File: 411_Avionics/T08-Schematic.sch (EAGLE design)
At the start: 41 parts, among them IC1 BQ24022, J1 USB-MICROB, J3 JST-PH-2-SMT-RA, U1 LP5907, U2 M25P10-AVMN6TP_TR, U3 LSM9DS0, U5 LTC1998, U6 ATMEGA32U4-AU, X1 8MHz

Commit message: Layout Review #1 With Andrew:
-changed all 0805 packages to 0603  (made a lot more room)
-made vias significantly smaller (made a lot more room)
-updated layout to reflect these changes, no DRC issues

We should consider hooking up the status pins of our battery charger to
LEDs.  Should also consider increasing the value of our current limiting
resistors from the processor.
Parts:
- C1, C10, C11, C12, C13, C14, C15, C16, C17, C18, C3, C4, C5, C6, C7, C8, C9: device rcl:C-EUC0805 -> rcl:C-EUC0603
- R1, R10, R11, R3, R4, R5, R6, R7, R8, R9: device rcl:R-US_R0805 -> rcl:R-US_R0603

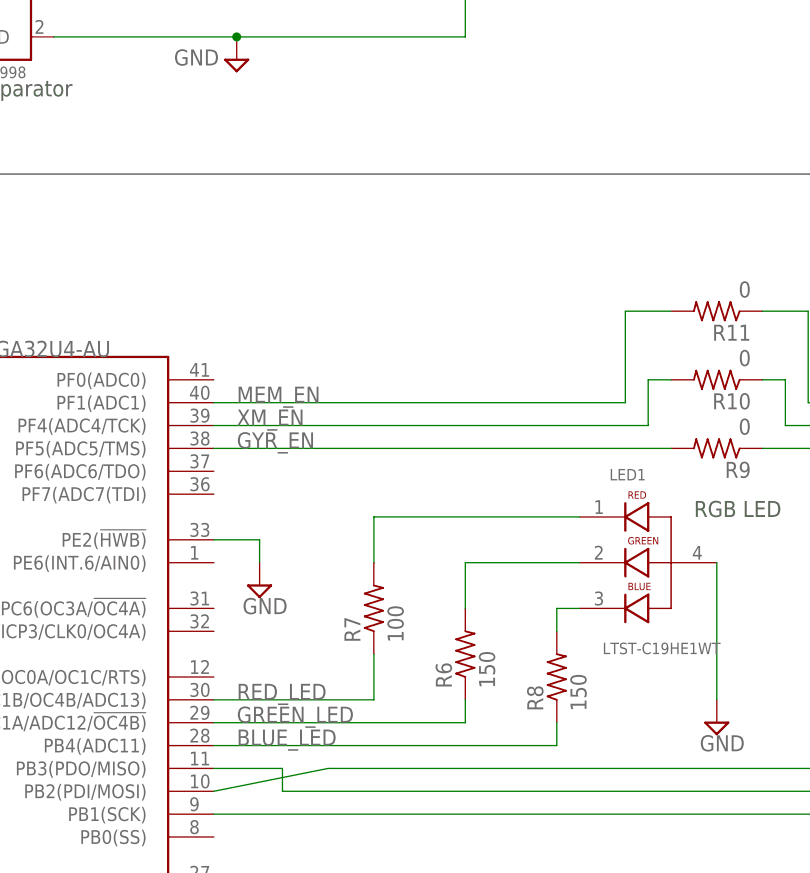
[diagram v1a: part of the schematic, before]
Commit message: Added 3-pin pad for firing circuit
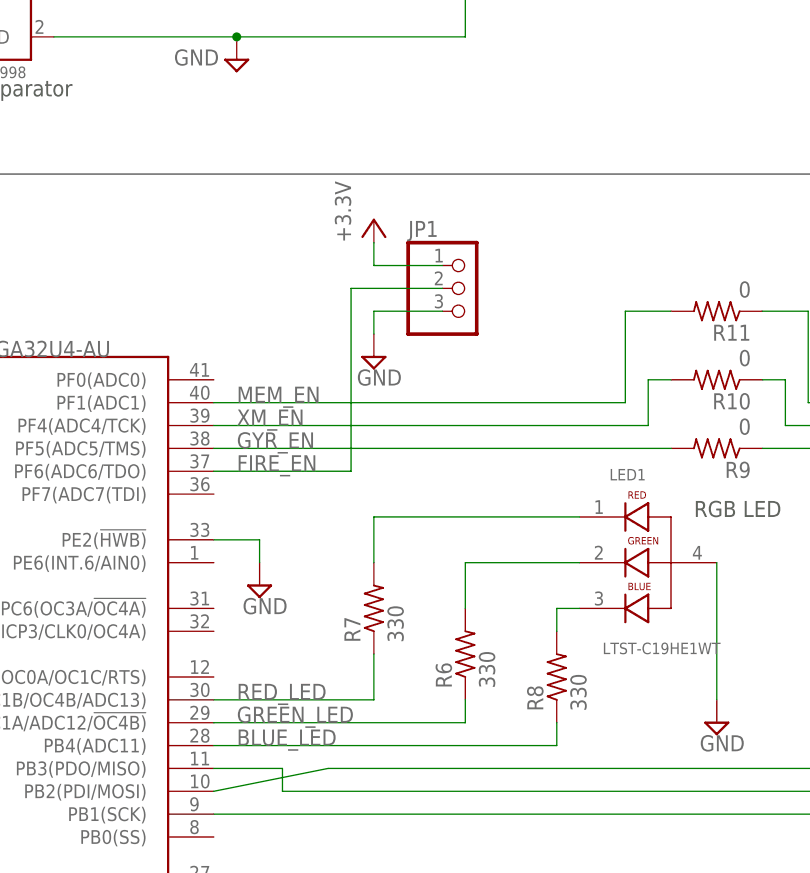
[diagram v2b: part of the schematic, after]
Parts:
- added JP1: (no value), pinhead:PINHD-1X3
- R6, R8: value 150 -> 330
- R7: value 100 -> 330
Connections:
- new net FIRE_EN: JP1.2, U6.PF6(ADC6/TDO)
- net GND: now also JP1.3
- net VCC: now also JP1.1
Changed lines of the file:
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@@
 <grid distance="0.1" unitdist="inch" unit="inch" style="lines" multiple="1" display="no" altdistance="0.01" altunitdist="inch" altunit="inch"/>
 <layers>
-<layer number="1" name="Top" color="4" fill="1" visible="yes" active="no"/>
-<layer number="16" name="Bottom" color="1" fill="1" visible="yes" active="no"/>
-<layer number="17" name="Pads" color="2" fill="1" visible="yes" active="no"/>
-<layer number="18" name="Vias" color="2" fill="1" visible="yes" active="no"/>
-<layer number="19" name="Unrouted" color="6" fill="1" visible="yes" active="no"/>
-<layer number="20" name="Dimension" color="15" fill="1" visible="yes" active="no"/>
-<layer number="21" name="tPlace" color="7" fill="1" visible="yes" active="no"/>
-<layer number="22" name="bPlace" color="7" fill="1" visible="yes" active="no"/>
-<layer number="23" name="tOrigins" color="15" fill="1" visible="yes" active="no"/>
-<layer number="24" name="bOrigins" color="15" fill="1" visible="yes" active="no"/>
-<layer number="25" name="tNames" color="7" fill="1" visible="yes" active="no"/>
-<layer number="26" name="bNames" color="7" fill="1" visible="yes" active="no"/>
-<layer number="27" name="tValues" color="7" fill="1" visible="yes" active="no"/>
-<layer number="28" name="bValues" color="7" fill="1" visible="yes" active="no"/>
+<layer number="1" name="Top" color="4" fill="1" visible="no" active="no"/>
+<layer number="16" name="Bottom" color="1" fill="1" visible="no" active="no"/>
+<layer number="17" name="Pads" color="2" fill="1" visible="no" active="no"/>
+<layer number="18" name="Vias" color="2" fill="1" visible="no" active="no"/>
+<layer number="19" name="Unrouted" color="6" fill="1" visible="no" active="no"/>
+<layer number="20" name="Dimension" color="15" fill="1" visible="no" active="no"/>
+<layer number="21" name="tPlace" color="7" fill="1" visible="no" active="no"/>
+<layer number="22" name="bPlace" color="7" fill="1" visible="no" active="no"/>
+<layer number="23" name="tOrigins" color="15" fill="1" visible="no" active="no"/>
+<layer number="24" name="bOrigins" color="15" fill="1" visible="no" active="no"/>
+<layer number="25" name="tNames" color="7" fill="1" visible="no" active="no"/>
+<layer number="26" name="bNames" color="7" fill="1" visible="no" active="no"/>
+<layer number="27" name="tValues" color="7" fill="1" visible="no" active="no"/>
+<layer number="28" name="bValues" color="7" fill="1" visible="no" active="no"/>
 <layer number="29" name="tStop" color="7" fill="3" visible="no" active="no"/>
 <layer number="30" name="bStop" color="7" fill="6" visible="no" active="no"/>
@@
 <layer number="35" name="tGlue" color="7" fill="4" visible="no" active="no"/>
 <layer number="36" name="bGlue" color="7" fill="5" visible="no" active="no"/>
-<layer number="37" name="tTest" color="7" fill="1" visible="yes" active="no"/>
-<layer number="38" name="bTest" color="7" fill="1" visible="yes" active="no"/>
+<layer number="37" name="tTest" color="7" fill="1" visible="no" active="no"/>
+<layer number="38" name="bTest" color="7" fill="1" visible="no" active="no"/>
 <layer number="39" name="tKeepout" color="4" fill="11" visible="no" active="no"/>
 <layer number="40" name="bKeepout" color="1" fill="11" visible="no" active="no"/>
@@
 <layer number="44" name="Drills" color="7" fill="1" visible="no" active="no"/>
 <layer number="45" name="Holes" color="7" fill="1" visible="no" active="no"/>
-<layer number="46" name="Milling" color="3" fill="1" visible="yes" active="no"/>
-<layer number="47" name="Measures" color="7" fill="1" visible="yes" active="no"/>
-<layer number="48" name="Document" color="7" fill="1" visible="yes" active="no"/>
-<layer number="49" name="Reference" color="7" fill="1" visible="yes" active="no"/>
-<layer number="50" name="dxf" color="7" fill="1" visible="yes" active="no"/>
-<layer number="51" name="tDocu" color="7" fill="1" visible="yes" active="no"/>
-<layer number="52" name="bDocu" color="7" fill="1" visible="yes" active="no"/>
-<layer number="53" name="tGND_GNDA" color="7" fill="9" visible="yes" active="no"/>
-<layer number="54" name="bGND_GNDA" color="1" fill="9" visible="yes" active="no"/>
-<layer number="56" name="wert" color="7" fill="1" visible="yes" active="no"/>
-<layer number="57" name="tCAD" color="7" fill="1" visible="yes" active="no"/>
-<layer number="59" name="tCarbon" color="7" fill="1" visible="yes" active="no"/>
-<layer number="60" name="bCarbon" color="7" fill="1" visible="yes" active="no"/>
+<layer number="46" name="Milling" color="3" fill="1" visible="no" active="no"/>
+<layer number="47" name="Measures" color="7" fill="1" visible="no" active="no"/>
+<layer number="48" name="Document" color="7" fill="1" visible="no" active="no"/>
+<layer number="49" name="Reference" color="7" fill="1" visible="no" active="no"/>
+<layer number="50" name="dxf" color="7" fill="1" visible="no" active="no"/>
+<layer number="51" name="tDocu" color="7" fill="1" visible="no" active="no"/>
+<layer number="52" name="bDocu" color="7" fill="1" visible="no" active="no"/>
+<layer number="53" name="tGND_GNDA" color="7" fill="9" visible="no" active="no"/>
+<layer number="54" name="bGND_GNDA" color="1" fill="9" visible="no" active="no"/>
+<layer number="56" name="wert" color="7" fill="1" visible="no" active="no"/>
+<layer number="57" name="tCAD" color="7" fill="1" visible="no" active="no"/>
+<layer number="59" name="tCarbon" color="7" fill="1" visible="no" active="no"/>
+<layer number="60" name="bCarbon" color="7" fill="1" visible="no" active="no"/>
 <layer number="90" name="Modules" color="5" fill="1" visible="yes" active="yes"/>
 <layer number="91" name="Nets" color="2" fill="1" visible="yes" active="yes"/>
@@
 </part>
 <part name="SUPPLY23" library="supply2" deviceset="GND" device=""/>
-<part name="R6" library="rcl" deviceset="R-US_" device="R0603" value="150"/>
-<part name="R7" library="rcl" deviceset="R-US_" device="R0603" value="100"/>
-<part name="R8" library="rcl" deviceset="R-US_" device="R0603" value="150"/>
+<part name="R6" library="rcl" deviceset="R-US_" device="R0603" value="330"/>
+<part name="R7" library="rcl" deviceset="R-US_" device="R0603" value="330"/>
+<part name="R8" library="rcl" deviceset="R-US_" device="R0603" value="330"/>
 <part name="R9" library="rcl" deviceset="R-US_" device="R0603" value="0"/>
 <part name="R10" library="rcl" deviceset="R-US_" device="R0603" value="0"/>
@@
 <part name="R1" library="rcl" deviceset="R-US_" device="R0603" value="4k"/>
 <part name="R2" library="rcl" deviceset="R-US_" device="R0805" value="10k"/>
+<part name="JP1" library="pinhead" deviceset="PINHD-1X3" device=""/>
+<part name="SUPPLY24" library="supply2" deviceset="GND" device=""/>
+<part name="P+7" library="supply1" deviceset="VCC" device="" value="+3.3V"/>
 </parts>
 <sheets>
@@
 <instance part="R1" gate="G$1" x="78.74" y="231.14" rot="R90"/>
 <instance part="R2" gate="G$1" x="119.38" y="182.88" rot="R90"/>
+<instance part="JP1" gate="A" x="203.2" y="185.42"/>
+<instance part="SUPPLY24" gate="GND" x="193.04" y="177.8"/>
+<instance part="P+7" gate="VCC" x="193.04" y="193.04"/>
 </instances>
 <busses>
@@
 <pinref part="SUPPLY7" gate="GND" pin="GND"/>
 <pinref part="R1" gate="G$1" pin="1"/>
+</segment>
+<segment>
+<pinref part="JP1" gate="A" pin="3"/>
+<wire x1="200.66" y1="182.88" x2="193.04" y2="182.88" width="0.1524" layer="91"/>
+<pinref part="SUPPLY24" gate="GND" pin="GND"/>
+<wire x1="193.04" y1="182.88" x2="193.04" y2="180.34" width="0.1524" layer="91"/>
 </segment>
 </net>
@@
 <pinref part="R2" gate="G$1" pin="2"/>
 </segment>
+<segment>
+<pinref part="JP1" gate="A" pin="1"/>
+<wire x1="200.66" y1="187.96" x2="193.04" y2="187.96" width="0.1524" layer="91"/>
+<wire x1="193.04" y1="187.96" x2="193.04" y2="190.5" width="0.1524" layer="91"/>
+<pinref part="P+7" gate="VCC" pin="VCC"/>
+</segment>
 </net>
 <net name="GYR_EN" class="0">
@@
 </segment>
 </net>
+<net name="FIRE_EN" class="0">
+<segment>
+<pinref part="U6" gate="G$1" pin="PF6(ADC6/TDO)"/>
+<wire x1="175.26" y1="165.1" x2="190.5" y2="165.1" width="0.1524" layer="91"/>
+<wire x1="190.5" y1="165.1" x2="190.5" y2="185.42" width="0.1524" layer="91"/>
+<label x="177.8" y="165.1" size="1.778" layer="95"/>
+<pinref part="JP1" gate="A" pin="2"/>
+<wire x1="190.5" y1="185.42" x2="200.66" y2="185.42" width="0.1524" layer="91"/>
+</segment>
+</net>

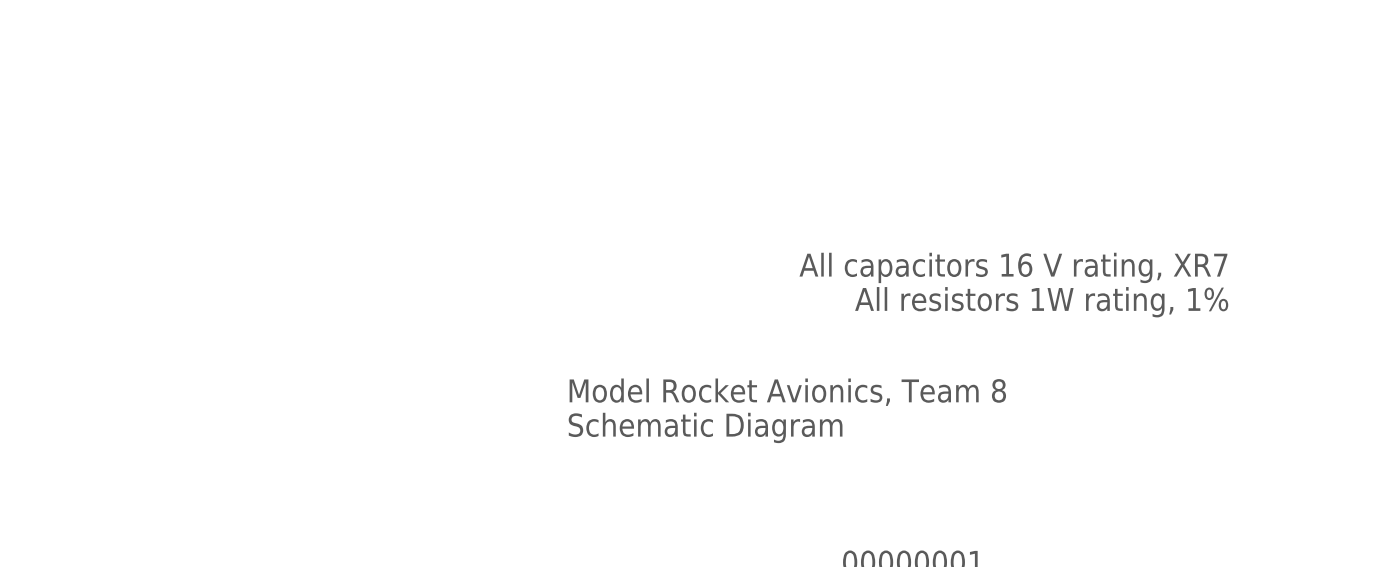
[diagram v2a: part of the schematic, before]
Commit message: Updated current limiting resistors to 0805 package.  Also fixed some oopsies on the layout (extra traces).
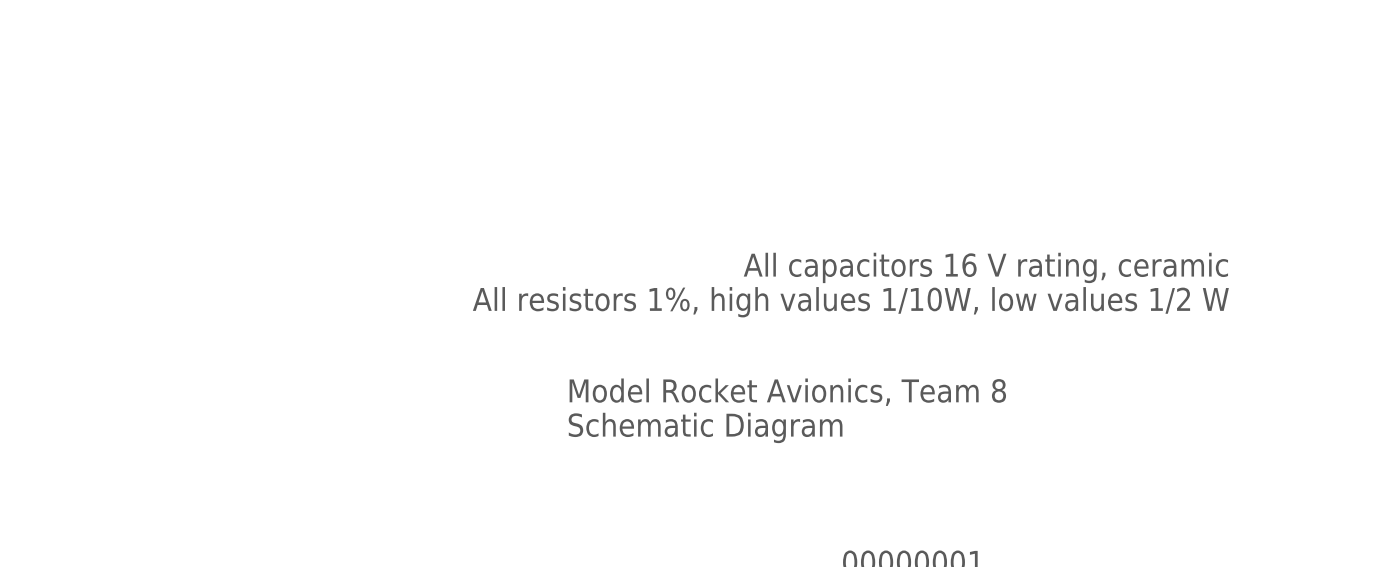
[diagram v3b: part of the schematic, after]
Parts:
- R6, R7, R8: device rcl:R-US_R0603 -> rcl:R-US_R0805
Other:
- note added: "All capacitors 16 V rating, ceramic All resistors 1%, high values 1/10W, low values 1/2 W"
- note removed: "All capacitors 16 V rating, XR7 All resistors 1W rating, 1%"
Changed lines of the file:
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@@
 <grid distance="0.1" unitdist="inch" unit="inch" style="lines" multiple="1" display="no" altdistance="0.01" altunitdist="inch" altunit="inch"/>
 <layers>
-<layer number="1" name="Top" color="4" fill="1" visible="no" active="no"/>
-<layer number="16" name="Bottom" color="1" fill="1" visible="no" active="no"/>
-<layer number="17" name="Pads" color="2" fill="1" visible="no" active="no"/>
-<layer number="18" name="Vias" color="2" fill="1" visible="no" active="no"/>
-<layer number="19" name="Unrouted" color="6" fill="1" visible="no" active="no"/>
-<layer number="20" name="Dimension" color="15" fill="1" visible="no" active="no"/>
-<layer number="21" name="tPlace" color="7" fill="1" visible="no" active="no"/>
-<layer number="22" name="bPlace" color="7" fill="1" visible="no" active="no"/>
-<layer number="23" name="tOrigins" color="15" fill="1" visible="no" active="no"/>
-<layer number="24" name="bOrigins" color="15" fill="1" visible="no" active="no"/>
-<layer number="25" name="tNames" color="7" fill="1" visible="no" active="no"/>
-<layer number="26" name="bNames" color="7" fill="1" visible="no" active="no"/>
-<layer number="27" name="tValues" color="7" fill="1" visible="no" active="no"/>
-<layer number="28" name="bValues" color="7" fill="1" visible="no" active="no"/>
+<layer number="1" name="Top" color="4" fill="1" visible="yes" active="no"/>
+<layer number="16" name="Bottom" color="1" fill="1" visible="yes" active="no"/>
+<layer number="17" name="Pads" color="2" fill="1" visible="yes" active="no"/>
+<layer number="18" name="Vias" color="2" fill="1" visible="yes" active="no"/>
+<layer number="19" name="Unrouted" color="6" fill="1" visible="yes" active="no"/>
+<layer number="20" name="Dimension" color="15" fill="1" visible="yes" active="no"/>
+<layer number="21" name="tPlace" color="7" fill="1" visible="yes" active="no"/>
+<layer number="22" name="bPlace" color="7" fill="1" visible="yes" active="no"/>
+<layer number="23" name="tOrigins" color="15" fill="1" visible="yes" active="no"/>
+<layer number="24" name="bOrigins" color="15" fill="1" visible="yes" active="no"/>
+<layer number="25" name="tNames" color="7" fill="1" visible="yes" active="no"/>
+<layer number="26" name="bNames" color="7" fill="1" visible="yes" active="no"/>
+<layer number="27" name="tValues" color="7" fill="1" visible="yes" active="no"/>
+<layer number="28" name="bValues" color="7" fill="1" visible="yes" active="no"/>
 <layer number="29" name="tStop" color="7" fill="3" visible="no" active="no"/>
 <layer number="30" name="bStop" color="7" fill="6" visible="no" active="no"/>
@@
 <layer number="35" name="tGlue" color="7" fill="4" visible="no" active="no"/>
 <layer number="36" name="bGlue" color="7" fill="5" visible="no" active="no"/>
-<layer number="37" name="tTest" color="7" fill="1" visible="no" active="no"/>
-<layer number="38" name="bTest" color="7" fill="1" visible="no" active="no"/>
+<layer number="37" name="tTest" color="7" fill="1" visible="yes" active="no"/>
+<layer number="38" name="bTest" color="7" fill="1" visible="yes" active="no"/>
 <layer number="39" name="tKeepout" color="4" fill="11" visible="no" active="no"/>
 <layer number="40" name="bKeepout" color="1" fill="11" visible="no" active="no"/>
@@
 <layer number="44" name="Drills" color="7" fill="1" visible="no" active="no"/>
 <layer number="45" name="Holes" color="7" fill="1" visible="no" active="no"/>
-<layer number="46" name="Milling" color="3" fill="1" visible="no" active="no"/>
-<layer number="47" name="Measures" color="7" fill="1" visible="no" active="no"/>
-<layer number="48" name="Document" color="7" fill="1" visible="no" active="no"/>
-<layer number="49" name="Reference" color="7" fill="1" visible="no" active="no"/>
-<layer number="50" name="dxf" color="7" fill="1" visible="no" active="no"/>
-<layer number="51" name="tDocu" color="7" fill="1" visible="no" active="no"/>
-<layer number="52" name="bDocu" color="7" fill="1" visible="no" active="no"/>
-<layer number="53" name="tGND_GNDA" color="7" fill="9" visible="no" active="no"/>
-<layer number="54" name="bGND_GNDA" color="1" fill="9" visible="no" active="no"/>
-<layer number="56" name="wert" color="7" fill="1" visible="no" active="no"/>
-<layer number="57" name="tCAD" color="7" fill="1" visible="no" active="no"/>
-<layer number="59" name="tCarbon" color="7" fill="1" visible="no" active="no"/>
-<layer number="60" name="bCarbon" color="7" fill="1" visible="no" active="no"/>
+<layer number="46" name="Milling" color="3" fill="1" visible="yes" active="no"/>
+<layer number="47" name="Measures" color="7" fill="1" visible="yes" active="no"/>
+<layer number="48" name="Document" color="7" fill="1" visible="yes" active="no"/>
+<layer number="49" name="Reference" color="7" fill="1" visible="yes" active="no"/>
+<layer number="50" name="dxf" color="7" fill="1" visible="yes" active="no"/>
+<layer number="51" name="tDocu" color="7" fill="1" visible="yes" active="no"/>
+<layer number="52" name="bDocu" color="7" fill="1" visible="yes" active="no"/>
+<layer number="53" name="tGND_GNDA" color="7" fill="9" visible="yes" active="no"/>
+<layer number="54" name="bGND_GNDA" color="1" fill="9" visible="yes" active="no"/>
+<layer number="56" name="wert" color="7" fill="1" visible="yes" active="no"/>
+<layer number="57" name="tCAD" color="7" fill="1" visible="yes" active="no"/>
+<layer number="59" name="tCarbon" color="7" fill="1" visible="yes" active="no"/>
+<layer number="60" name="bCarbon" color="7" fill="1" visible="yes" active="no"/>
 <layer number="90" name="Modules" color="5" fill="1" visible="yes" active="yes"/>
 <layer number="91" name="Nets" color="2" fill="1" visible="yes" active="yes"/>
@@
 </part>
 <part name="SUPPLY23" library="supply2" deviceset="GND" device=""/>
-<part name="R6" library="rcl" deviceset="R-US_" device="R0603" value="330"/>
-<part name="R7" library="rcl" deviceset="R-US_" device="R0603" value="330"/>
-<part name="R8" library="rcl" deviceset="R-US_" device="R0603" value="330"/>
+<part name="R6" library="rcl" deviceset="R-US_" device="R0805" value="330"/>
+<part name="R7" library="rcl" deviceset="R-US_" device="R0805" value="330"/>
+<part name="R8" library="rcl" deviceset="R-US_" device="R0805" value="330"/>
 <part name="R9" library="rcl" deviceset="R-US_" device="R0603" value="0"/>
 <part name="R10" library="rcl" deviceset="R-US_" device="R0603" value="0"/>
@@
 <text x="261.62" y="195.58" size="1.778" layer="97">Sensors</text>
 <text x="261.62" y="236.22" size="1.778" layer="97">Flash Memory</text>
-<text x="403.86" y="45.72" size="2.54" layer="97" rot="R180">All capacitors 16 V rating, XR7
-All resistors 1W rating, 1%</text>
+<text x="403.86" y="45.72" size="2.54" layer="97" rot="R180">All capacitors 16 V rating, ceramic
+All resistors 1%, high values 1/10W, low values 1/2 W</text>
 <text x="91.44" y="210.82" size="1.778" layer="97" rot="R90">Battery Connector</text>
 <wire x1="17.78" y1="264.16" x2="17.78" y2="198.12" width="0.1524" layer="97"/>
